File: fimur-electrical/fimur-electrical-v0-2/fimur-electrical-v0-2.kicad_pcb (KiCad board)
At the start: 2 copper layers, 20 parts, among them J1 Conn_01x16, J10 Conn_01x04, J11 Conn_01x04, J12 Conn_01x04, J13 Conn_01x04, J14 Conn_01x04, J15 Conn_01x04, J17 Conn_02x02_Odd_Even, J2 Conn_01x16, J3 Conn_01x03_Pin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

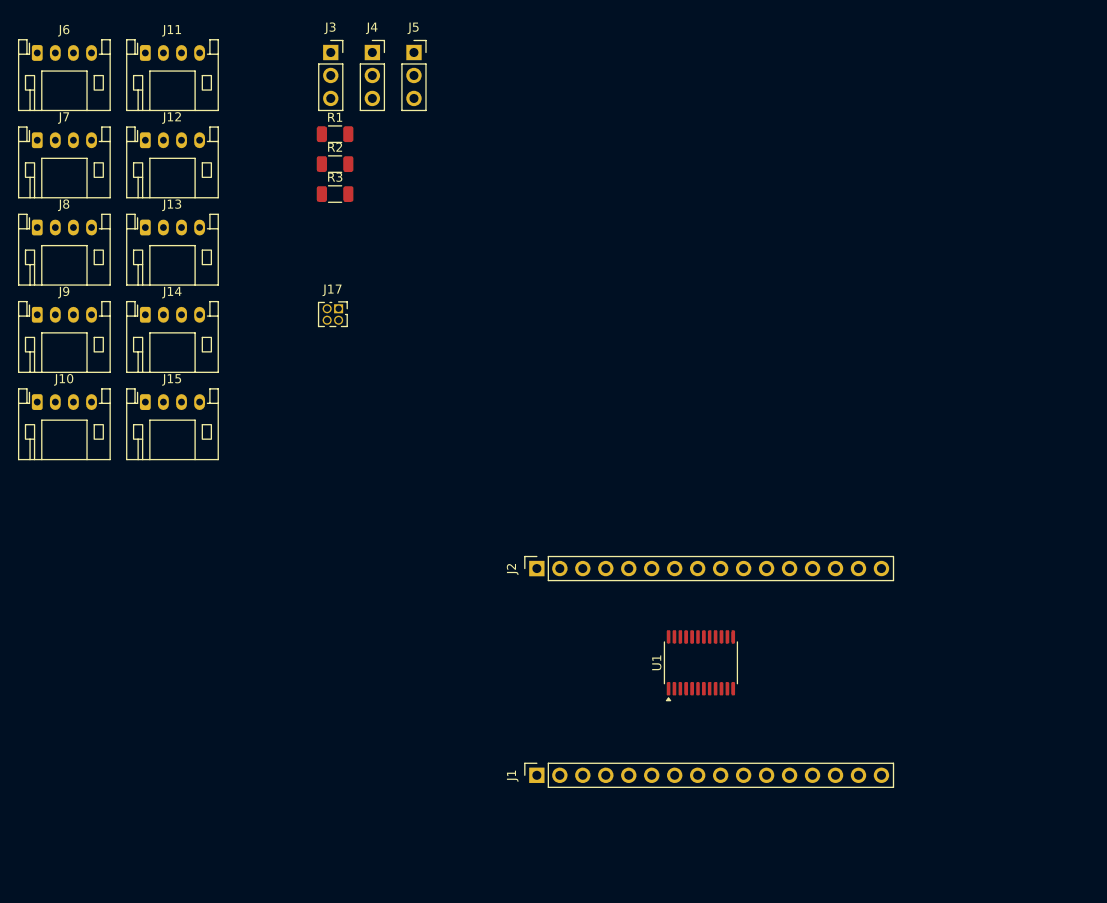
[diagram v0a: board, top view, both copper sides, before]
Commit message: multiplex schematic and layout and standardization with 2-imu board
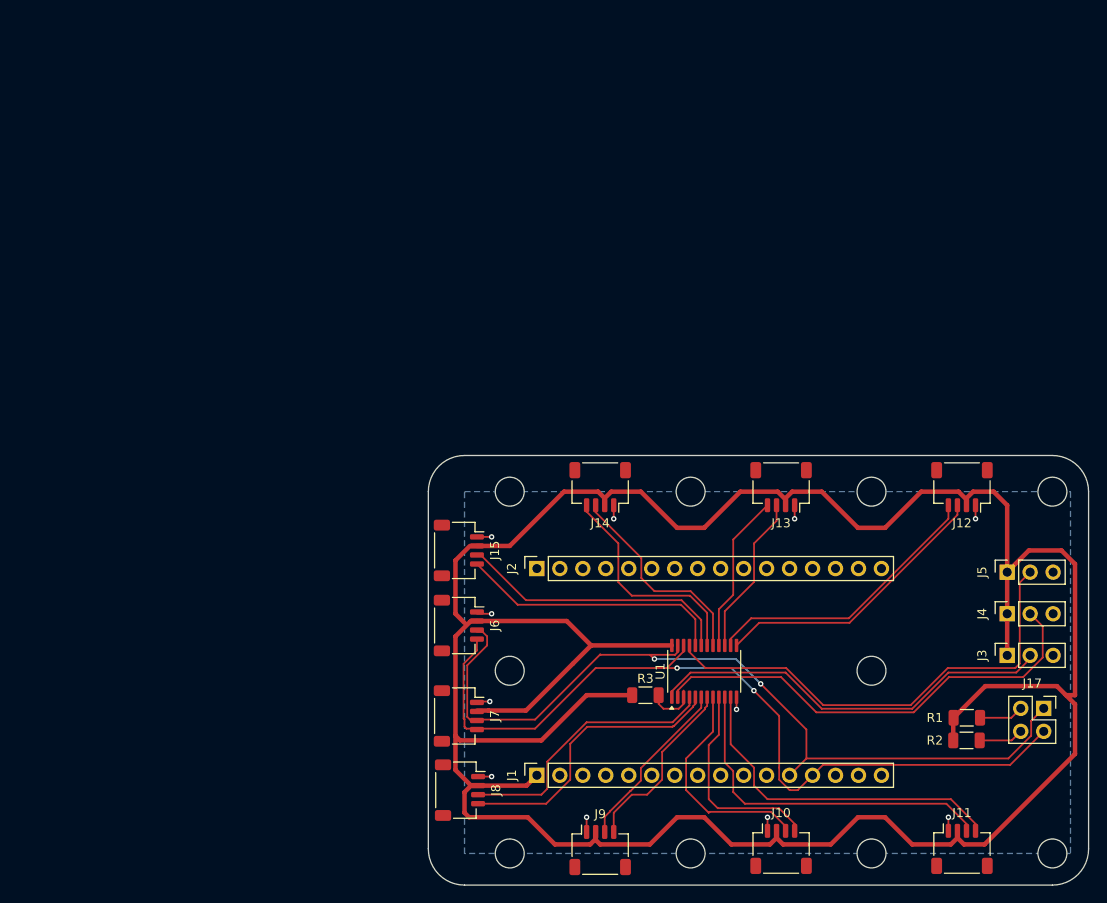
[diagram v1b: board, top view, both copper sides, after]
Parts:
- added REF**: MountingHole_3.2mm_M3, MountingHole:MountingHole_3.2mm_M3, F.Cu at (117.0, 131.5)
- added REF**: MountingHole_3.2mm_M3, MountingHole:MountingHole_3.2mm_M3, F.Cu at (97.0, 131.5)
- added REF**: MountingHole_3.2mm_M3, MountingHole:MountingHole_3.2mm_M3, F.Cu at (137.0, 91.5)
- added REF**: MountingHole_3.2mm_M3, MountingHole:MountingHole_3.2mm_M3, F.Cu at (137.0, 111.3)
- added REF**: MountingHole_3.2mm_M3, MountingHole:MountingHole_3.2mm_M3, F.Cu at (97.0, 111.3)
- added REF**: MountingHole_3.2mm_M3, MountingHole:MountingHole_3.2mm_M3, F.Cu at (117.0, 91.5)
- added REF**: MountingHole_3.2mm_M3, MountingHole:MountingHole_3.2mm_M3, F.Cu at (157.0, 131.5)
- added REF**: MountingHole_3.2mm_M3, MountingHole:MountingHole_3.2mm_M3, F.Cu at (137.0, 131.5)
- added REF**: MountingHole_3.2mm_M3, MountingHole:MountingHole_3.2mm_M3, F.Cu at (97.0, 91.5)
- added REF**: MountingHole_3.2mm_M3, MountingHole:MountingHole_3.2mm_M3, F.Cu at (157.0, 91.5)
- J10: renamed from J9; footprint Connector_JST:JST_PH_S4B-PH-K_1x04_P2.00mm_Horizontal -> Connector_JST:JST_SH_SM04B-SRSS-TB_1x04-1MP_P1.00mm_Horizontal
- J11: renamed from J10; footprint Connector_JST:JST_PH_S4B-PH-K_1x04_P2.00mm_Horizontal -> Connector_JST:JST_SH_SM04B-SRSS-TB_1x04-1MP_P1.00mm_Horizontal
- J12: renamed from J11; footprint Connector_JST:JST_PH_S4B-PH-K_1x04_P2.00mm_Horizontal -> Connector_JST:JST_SH_SM04B-SRSS-TB_1x04-1MP_P1.00mm_Horizontal
- J13: renamed from J12; footprint Connector_JST:JST_PH_S4B-PH-K_1x04_P2.00mm_Horizontal -> Connector_JST:JST_SH_SM04B-SRSS-TB_1x04-1MP_P1.00mm_Horizontal
- J14: renamed from J13; footprint Connector_JST:JST_PH_S4B-PH-K_1x04_P2.00mm_Horizontal -> Connector_JST:JST_SH_SM04B-SRSS-TB_1x04-1MP_P1.00mm_Horizontal
- J15: renamed from J14; footprint Connector_JST:JST_PH_S4B-PH-K_1x04_P2.00mm_Horizontal -> Connector_JST:JST_SH_SM04B-SRSS-TB_1x04-1MP_P1.00mm_Horizontal
- J17: footprint Connector_PinSocket_1.27mm:PinSocket_2x02_P1.27mm_Vertical -> Connector_PinSocket_2.54mm:PinSocket_2x02_P2.54mm_Vertical
- J6: footprint Connector_JST:JST_PH_S4B-PH-K_1x04_P2.00mm_Horizontal -> Connector_JST:JST_SH_SM04B-SRSS-TB_1x04-1MP_P1.00mm_Horizontal
- J7: renamed from J15; footprint Connector_JST:JST_PH_S4B-PH-K_1x04_P2.00mm_Horizontal -> Connector_JST:JST_SH_SM04B-SRSS-TB_1x04-1MP_P1.00mm_Horizontal
- J8: renamed from J7; footprint Connector_JST:JST_PH_S4B-PH-K_1x04_P2.00mm_Horizontal -> Connector_JST:JST_SH_SM04B-SRSS-TB_1x04-1MP_P1.00mm_Horizontal
- J9: renamed from J8; footprint Connector_JST:JST_PH_S4B-PH-K_1x04_P2.00mm_Horizontal -> Connector_JST:JST_SH_SM04B-SRSS-TB_1x04-1MP_P1.00mm_Horizontal
- moved J11 113.5 mm to (147.0, 131.0)
- moved J12 102.3 mm to (147.0, 91.0), turned to 180 degrees
- moved J10 101.2 mm to (127.0, 131.0)
- moved J3 100.2 mm to (152.0, 109.6), turned to 90 degrees
- moved R1 95.1 mm to (147.5, 116.5)
- moved R2 94.5 mm to (147.5, 119.0)
- moved J4 93.7 mm to (152.0, 105.0), turned to 90 degrees
- moved J9 92.8 mm to (107.0, 131.1)
- moved J17 89.6 mm to (156.0, 115.5)
- moved J5 87.2 mm to (152.0, 100.4), turned to 90 degrees
- moved J8 85.7 mm to (91.5, 124.5), turned to -90 degrees
- moved J13 80.1 mm to (127.0, 91.0), turned to 180 degrees
- moved J6 78.6 mm to (91.4, 106.3), turned to -90 degrees
- moved R3 65.2 mm to (112.0, 114.0)
- moved J14 57.9 mm to (107.0, 91.0), turned to 180 degrees
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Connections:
- net Net-(J1-3V3) renamed VCC
- net Net-(J1-G) renamed GND
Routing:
- net VCC: track 0.00 -> 324.3 mm
- net Net-(J1-2): track 0.00 -> 94.4 mm, vias 0 -> 2
- net Net-(J1-3): track 0.00 -> 93.4 mm, vias 0 -> 2
- net Net-(J5-Pin_2): track 0.00 -> 52.2 mm
- net Net-(J4-Pin_2): track 0.00 -> 51.2 mm
- net Net-(J3-Pin_2): track 0.00 -> 45.4 mm
- net Net-(J11-Pin_3): track 0.00 -> 38.9 mm
- net Net-(J11-Pin_4): track 0.00 -> 37.9 mm
- net Net-(J12-Pin_4): track 0.00 -> 31.8 mm
- net Net-(J8-Pin_4): track 0.00 -> 31.7 mm
- net Net-(J12-Pin_3): track 0.00 -> 31.5 mm
- net Net-(J15-Pin_3): track 0.00 -> 30.6 mm
- net Net-(J8-Pin_3): track 0.00 -> 30.1 mm
- net Net-(J15-Pin_4): track 0.00 -> 29.6 mm
- net Net-(J14-Pin_4): track 0.00 -> 24.8 mm
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- added copper zone on B.Cu, net GND
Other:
- board outline added: 73 x 47.5 mm
